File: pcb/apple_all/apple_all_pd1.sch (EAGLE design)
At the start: 47 parts, among them IC1 STM32F072C8T6, SW1 324_SW, SW2 324_SW, SW3 324_SW

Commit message: updated PCB
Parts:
- added TP1, TP2, TP3: PTR1TP14R, testpad:PTR1TP14R
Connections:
- new net N$10: IC1PORTB_L.PB5, JP2.2
- new net N$20: IC1PORTC.PC15, TP1.TP
- new net N$41: IC1PORTF/OSC.PF0/OSC<=, TP2.TP
- new net N$42: IC1PORTF/OSC.PF1/OSC=>, TP3.TP
- net N$24: no longer JP6.EARTH-NORM
- net N$46: no longer IC1PORTB_L.PB5, JP2.2
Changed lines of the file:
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@@
 <part name="R6" library="SparkFun-Passives" deviceset="RESISTOR" device="0805-RES" value="2K"/>
 <part name="R17" library="SparkFun-Passives" deviceset="RESISTOR" device="0805-RES" value="100"/>
+<part name="TP2" library="testpad" library_urn="urn:adsk.eagle:library:385" deviceset="PTR1" device="TP14R" package3d_urn="urn:adsk.eagle:package:27966/1"/>
+<part name="TP1" library="testpad" library_urn="urn:adsk.eagle:library:385" deviceset="PTR1" device="TP14R" package3d_urn="urn:adsk.eagle:package:27966/1"/>
+<part name="TP3" library="testpad" library_urn="urn:adsk.eagle:library:385" deviceset="PTR1" device="TP14R" package3d_urn="urn:adsk.eagle:package:27966/1"/>
 </parts>
 <sheets>
@@
 <attribute name="VALUE" x="339.09" y="9.398" size="1.778" layer="96"/>
 </instance>
+<instance part="TP2" gate="G$1" x="213.36" y="-2.54" smashed="yes" rot="R90">
+<attribute name="NAME" x="219.71" y="-3.556" size="1.778" layer="95" rot="R180"/>
+<attribute name="TP_SIGNAL_NAME" x="215.9" y="-1.27" size="1.778" layer="97" rot="R90"/>
+</instance>
+<instance part="TP1" gate="G$1" x="210.82" y="10.16" smashed="yes" rot="R90">
+<attribute name="NAME" x="217.17" y="9.144" size="1.778" layer="95" rot="R180"/>
+<attribute name="TP_SIGNAL_NAME" x="213.36" y="11.43" size="1.778" layer="97" rot="R90"/>
+</instance>
+<instance part="TP3" gate="G$1" x="228.6" y="-5.08" smashed="yes" rot="R90">
+<attribute name="NAME" x="234.95" y="-6.096" size="1.778" layer="95" rot="R180"/>
+<attribute name="TP_SIGNAL_NAME" x="231.14" y="-3.81" size="1.778" layer="97" rot="R90"/>
+</instance>
 </instances>
 <busses>
@@
 <wire x1="66.04" y1="93.98" x2="66.04" y2="111.76" width="0.1524" layer="91"/>
 <pinref part="JP2" gate="G$1" pin="1"/>
-<wire x1="66.04" y1="45.72" x2="66.04" y2="91.44" width="0.1524" layer="91"/>
-<pinref part="IC1" gate="PORTB_L" pin="PB5"/>
-<wire x1="43.18" y1="45.72" x2="66.04" y2="45.72" width="0.1524" layer="91"/>
-<pinref part="JP2" gate="G$1" pin="2"/>
-<wire x1="66.04" y1="93.98" x2="66.04" y2="91.44" width="0.1524" layer="91"/>
-<junction x="66.04" y="93.98"/>
-<junction x="66.04" y="91.44"/>
 <pinref part="R6" gate="G$1" pin="1"/>
 <wire x1="-7.62" y1="127" x2="-27.94" y2="127" width="0.1524" layer="91"/>
@@
 <pinref part="R13" gate="G$1" pin="1"/>
 <wire x1="294.64" y1="20.32" x2="297.18" y2="20.32" width="0.1524" layer="91"/>
-<pinref part="JP6" gate="G$1" pin="EARTH-NORM"/>
-<wire x1="294.64" y1="17.78" x2="294.64" y2="20.32" width="0.1524" layer="91"/>
-<junction x="294.64" y="20.32"/>
 </segment>
 </net>
@@
 </segment>
 </net>
+<net name="N$10" class="0">
+<segment>
+<pinref part="JP2" gate="G$1" pin="2"/>
+<wire x1="66.04" y1="45.72" x2="66.04" y2="91.44" width="0.1524" layer="91"/>
+<pinref part="IC1" gate="PORTB_L" pin="PB5"/>
+<wire x1="43.18" y1="45.72" x2="66.04" y2="45.72" width="0.1524" layer="91"/>
+</segment>
+</net>
+<net name="N$20" class="0">
+<segment>
+<pinref part="IC1" gate="PORTC" pin="PC15"/>
+<pinref part="TP1" gate="G$1" pin="TP"/>
+<wire x1="185.42" y1="10.16" x2="208.28" y2="10.16" width="0.1524" layer="91"/>
+</segment>
+</net>
+<net name="N$41" class="0">
+<segment>
+<pinref part="IC1" gate="PORTF/OSC" pin="PF0/OSC&lt;="/>
+<pinref part="TP2" gate="G$1" pin="TP"/>
+<wire x1="185.42" y1="-2.54" x2="210.82" y2="-2.54" width="0.1524" layer="91"/>
+</segment>
+</net>
+<net name="N$42" class="0">
+<segment>
+<pinref part="IC1" gate="PORTF/OSC" pin="PF1/OSC=&gt;"/>
+<pinref part="TP3" gate="G$1" pin="TP"/>
+<wire x1="185.42" y1="-5.08" x2="226.06" y2="-5.08" width="0.1524" layer="91"/>
+</segment>
+</net>

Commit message: updated values
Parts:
- R11, R7: value 200 -> 100
- R18, R21, R6, R9: value 2K -> 5.1K
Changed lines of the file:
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@@
 <part name="+3V16" library="backplane" deviceset="+3V3" device=""/>
 <part name="LED1" library="adafruit" deviceset="LED" device="CHIP-LED0805"/>
-<part name="R9" library="SparkFun-Passives" deviceset="RESISTOR" device="0805-RES" value="2K"/>
+<part name="R9" library="SparkFun-Passives" deviceset="RESISTOR" device="0805-RES" value="5.1K"/>
 <part name="GND9" library="backplane" deviceset="GND" device=""/>
 <part name="C1" library="clock" deviceset="CAP" device="0805" value="100nF"/>
@@
 <part name="C3" library="clock" deviceset="CAP" device="0805" value="100nF"/>
 <part name="LED2" library="adafruit" deviceset="LED" device="CHIP-LED0805"/>
-<part name="R18" library="SparkFun-Passives" deviceset="RESISTOR" device="0805-RES" value="2K"/>
+<part name="R18" library="SparkFun-Passives" deviceset="RESISTOR" device="0805-RES" value="5.1K"/>
 <part name="GND16" library="SparkFun-Aesthetics" deviceset="GND" device=""/>
 <part name="+3V10" library="backplane" deviceset="+3V3" device=""/>
@@
 <part name="U$3" library="adafruit_changed" deviceset="PINHD1X4" device=""/>
 <part name="LED3" library="adafruit" deviceset="LED" device="CHIP-LED0805"/>
-<part name="R21" library="SparkFun-Passives" deviceset="RESISTOR" device="0805-RES" value="2K"/>
+<part name="R21" library="SparkFun-Passives" deviceset="RESISTOR" device="0805-RES" value="5.1K"/>
 <part name="GND21" library="supply1" library_urn="urn:adsk.eagle:library:371" deviceset="GND" device=""/>
 <part name="GND22" library="supply1" library_urn="urn:adsk.eagle:library:371" deviceset="GND" device=""/>
@@
 <part name="SUPPLY7" library="supply2" library_urn="urn:adsk.eagle:library:372" deviceset="+7V" device=""/>
 <part name="JP1" library="pinhead" library_urn="urn:adsk.eagle:library:325" deviceset="PINHD-1X5" device="" package3d_urn="urn:adsk.eagle:package:22469/2"/>
-<part name="R7" library="SparkFun-Passives" deviceset="RESISTOR" device="0805-RES" value="200"/>
-<part name="R11" library="SparkFun-Passives" deviceset="RESISTOR" device="0805-RES" value="200"/>
+<part name="R7" library="SparkFun-Passives" deviceset="RESISTOR" device="0805-RES" value="100"/>
+<part name="R11" library="SparkFun-Passives" deviceset="RESISTOR" device="0805-RES" value="100"/>
 <part name="JP3" library="pinhead" library_urn="urn:adsk.eagle:library:325" deviceset="PINHD-2X2" device="" package3d_urn="urn:adsk.eagle:package:22455/2"/>
 <part name="JP7" library="adafruit" deviceset="PINHD-1X6" device="CB"/>
@@
 <part name="GND19" library="supply1" library_urn="urn:adsk.eagle:library:371" deviceset="GND" device=""/>
 <part name="JP2" library="pinhead" library_urn="urn:adsk.eagle:library:325" deviceset="PINHD-1X2" device="" package3d_urn="urn:adsk.eagle:package:22435/2"/>
-<part name="R6" library="SparkFun-Passives" deviceset="RESISTOR" device="0805-RES" value="2K"/>
+<part name="R6" library="SparkFun-Passives" deviceset="RESISTOR" device="0805-RES" value="5.1K"/>
 <part name="R17" library="SparkFun-Passives" deviceset="RESISTOR" device="0805-RES" value="100"/>
 <part name="TP2" library="testpad" library_urn="urn:adsk.eagle:library:385" deviceset="PTR1" device="TP14R" package3d_urn="urn:adsk.eagle:package:27966/1"/>

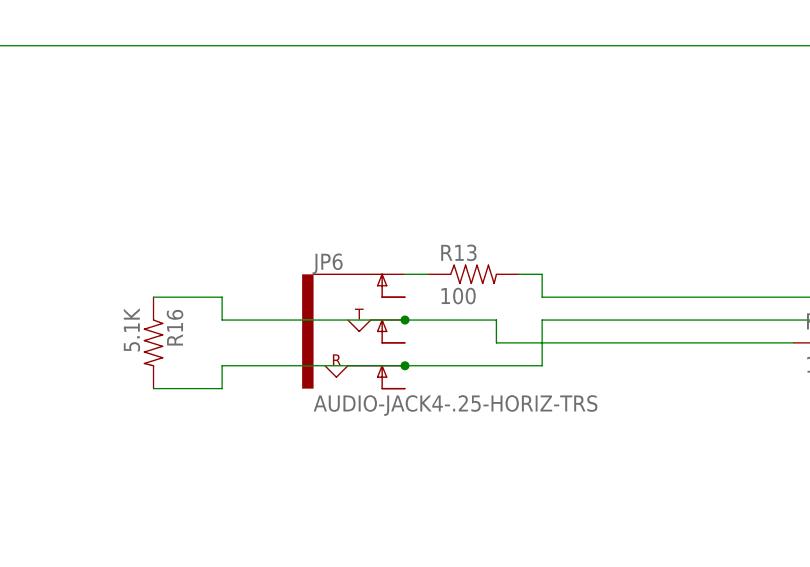
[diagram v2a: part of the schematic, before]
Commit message: moved resistors
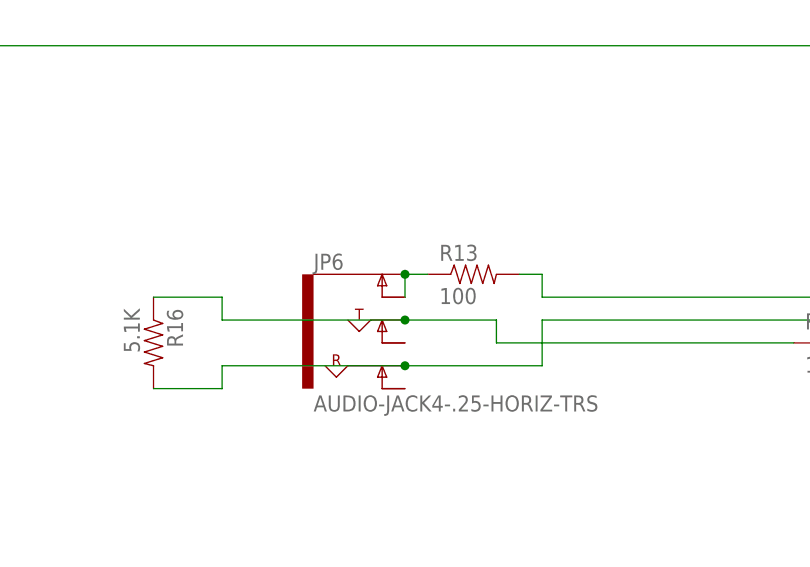
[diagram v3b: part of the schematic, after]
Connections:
- net N$24: now also JP6.EARTH-NORM
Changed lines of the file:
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@@
 <pinref part="R13" gate="G$1" pin="1"/>
 <wire x1="294.64" y1="20.32" x2="297.18" y2="20.32" width="0.1524" layer="91"/>
+<pinref part="JP6" gate="G$1" pin="EARTH-NORM"/>
+<wire x1="294.64" y1="17.78" x2="294.64" y2="20.32" width="0.1524" layer="91"/>
+<junction x="294.64" y="20.32"/>
 </segment>
 </net>

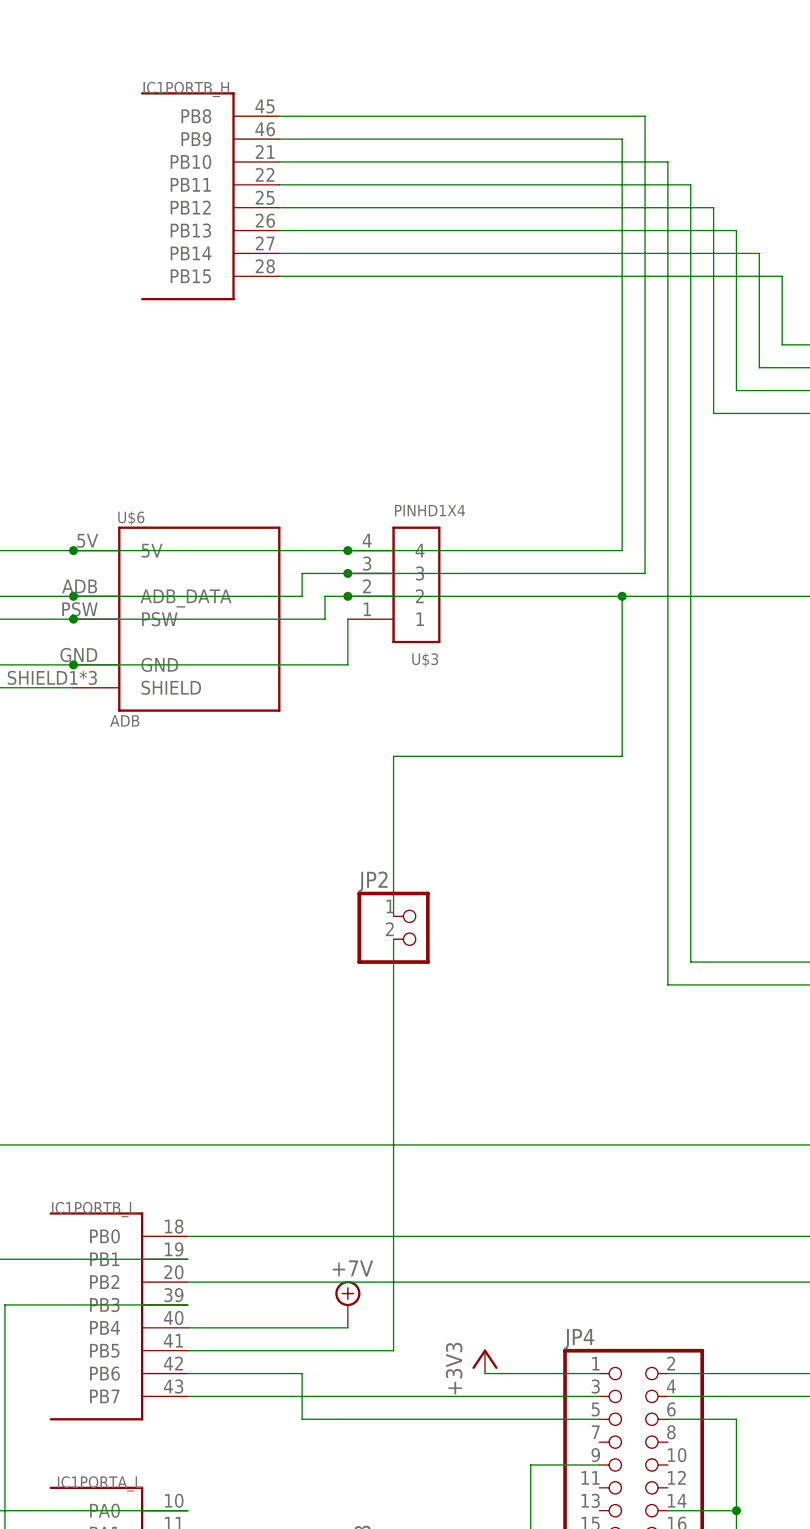
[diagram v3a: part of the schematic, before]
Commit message: added resistors on DET pins, cleaned up silkscreen
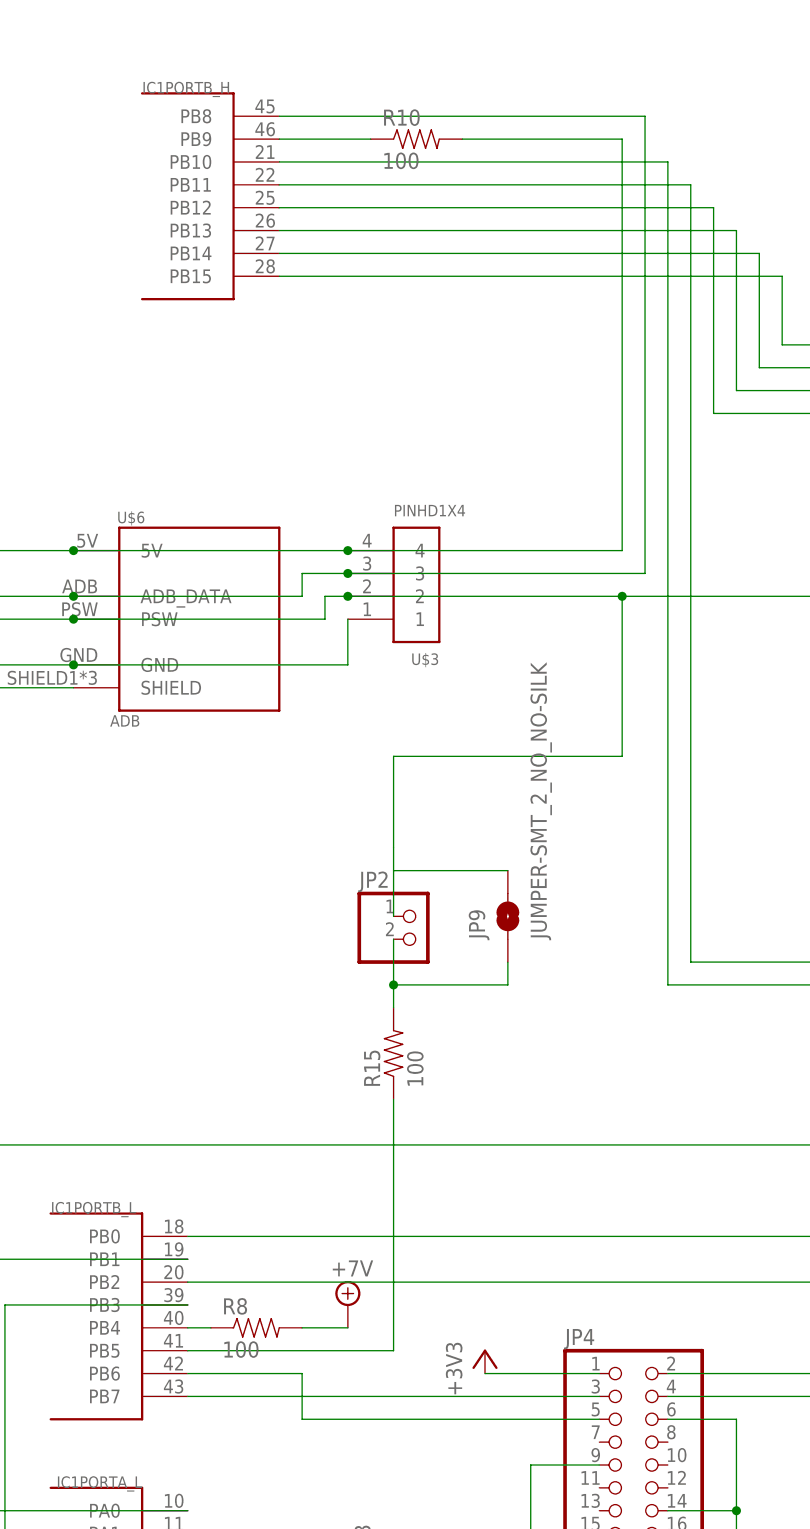
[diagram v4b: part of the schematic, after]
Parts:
- added JP9: JUMPER-SMT_2_NO_NO-SILK, SparkFun-Jumpers:JUMPER-SMT_2_NO_NO-SILK
- added R10, R15, R8: 100, SparkFun-Passives:RESISTOR0805-RES
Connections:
- new net N$44: IC1PORTB_L.PB4, R8.1
- new net N$45: IC1PORTB_H.PB9, R10.1
- new net N$47: JP2.2, JP9.1, R15.2
- net +7V: now also R8.2; no longer IC1PORTB_L.PB4
- net N$10: now also R15.1; no longer JP2.2
- net N$3: now also R10.2; no longer IC1PORTB_H.PB9
- net N$46: now also JP9.2
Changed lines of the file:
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@@
 <part name="TP1" library="testpad" library_urn="urn:adsk.eagle:library:385" deviceset="PTR1" device="TP14R" package3d_urn="urn:adsk.eagle:package:27966/1"/>
 <part name="TP3" library="testpad" library_urn="urn:adsk.eagle:library:385" deviceset="PTR1" device="TP14R" package3d_urn="urn:adsk.eagle:package:27966/1"/>
+<part name="R8" library="SparkFun-Passives" deviceset="RESISTOR" device="0805-RES" value="100"/>
+<part name="R10" library="SparkFun-Passives" deviceset="RESISTOR" device="0805-RES" value="100"/>
+<part name="R15" library="SparkFun-Passives" deviceset="RESISTOR" device="0805-RES" value="100"/>
+<part name="JP9" library="SparkFun-Jumpers" deviceset="JUMPER-SMT_2_NO" device="_NO-SILK"/>
 </parts>
 <sheets>
@@
 <attribute name="TP_SIGNAL_NAME" x="231.14" y="-3.81" size="1.778" layer="97" rot="R90"/>
 </instance>
+<instance part="R8" gate="G$1" x="50.8" y="48.26" smashed="yes">
+<attribute name="NAME" x="46.99" y="49.7586" size="1.778" layer="95"/>
+<attribute name="VALUE" x="46.99" y="44.958" size="1.778" layer="96"/>
+</instance>
+<instance part="R10" gate="G$1" x="68.58" y="180.34" smashed="yes">
+<attribute name="NAME" x="64.77" y="181.8386" size="1.778" layer="95"/>
+<attribute name="VALUE" x="64.77" y="177.038" size="1.778" layer="96"/>
+</instance>
+<instance part="R15" gate="G$1" x="66.04" y="78.74" smashed="yes" rot="R90">
+<attribute name="NAME" x="64.5414" y="74.93" size="1.778" layer="95" rot="R90"/>
+<attribute name="VALUE" x="69.342" y="74.93" size="1.778" layer="96" rot="R90"/>
+</instance>
+<instance part="JP9" gate="G$1" x="78.74" y="93.98" smashed="yes" rot="R90">
+<attribute name="NAME" x="76.2" y="91.44" size="1.778" layer="95" font="vector" rot="R90"/>
+<attribute name="VALUE" x="81.28" y="91.44" size="1.778" layer="96" font="vector" rot="R90" align="top-left"/>
+</instance>
 </instances>
 <busses>
@@
 <junction x="60.96" y="134.62"/>
 <wire x1="91.44" y1="134.62" x2="91.44" y2="180.34" width="0.1524" layer="91"/>
-<pinref part="IC1" gate="PORTB_H" pin="PB9"/>
-<wire x1="91.44" y1="180.34" x2="53.34" y2="180.34" width="0.1524" layer="91"/>
 <pinref part="R6" gate="G$1" pin="2"/>
 <wire x1="-7.62" y1="134.62" x2="-7.62" y2="137.16" width="0.1524" layer="91"/>
 <wire x1="-7.62" y1="137.16" x2="-27.94" y2="137.16" width="0.1524" layer="91"/>
 <junction x="-7.62" y="134.62"/>
+<wire x1="91.44" y1="180.34" x2="73.66" y2="180.34" width="0.1524" layer="91"/>
+<pinref part="R10" gate="G$1" pin="2"/>
 </segment>
 </net>
@@
 <junction x="91.44" y="129.54"/>
 <junction x="152.4" y="129.54"/>
-<wire x1="66.04" y1="93.98" x2="66.04" y2="111.76" width="0.1524" layer="91"/>
+<wire x1="66.04" y1="93.98" x2="66.04" y2="99.06" width="0.1524" layer="91"/>
 <pinref part="JP2" gate="G$1" pin="1"/>
 <pinref part="R6" gate="G$1" pin="1"/>
+<wire x1="66.04" y1="101.6" x2="66.04" y2="111.76" width="0.1524" layer="91"/>
 <wire x1="-7.62" y1="127" x2="-27.94" y2="127" width="0.1524" layer="91"/>
 <junction x="-7.62" y="127"/>
+<pinref part="JP9" gate="G$1" pin="2"/>
+<wire x1="78.74" y1="99.06" x2="66.04" y2="99.06" width="0.1524" layer="91"/>
+<wire x1="66.04" y1="99.06" x2="66.04" y2="101.6" width="0.1524" layer="91"/>
 </segment>
 </net>
@@
 </segment>
 <segment>
-<pinref part="IC1" gate="PORTB_L" pin="PB4"/>
-<wire x1="43.18" y1="48.26" x2="60.96" y2="48.26" width="0.1524" layer="91"/>
 <pinref part="SUPPLY1" gate="G$1" pin="+7V"/>
+<wire x1="55.88" y1="48.26" x2="60.96" y2="48.26" width="0.1524" layer="91"/>
+<pinref part="R8" gate="G$1" pin="2"/>
 </segment>
 </net>
@@
 <net name="N$10" class="0">
 <segment>
-<pinref part="JP2" gate="G$1" pin="2"/>
-<wire x1="66.04" y1="45.72" x2="66.04" y2="91.44" width="0.1524" layer="91"/>
 <pinref part="IC1" gate="PORTB_L" pin="PB5"/>
 <wire x1="43.18" y1="45.72" x2="66.04" y2="45.72" width="0.1524" layer="91"/>
+<wire x1="66.04" y1="45.72" x2="66.04" y2="73.66" width="0.1524" layer="91"/>
+<pinref part="R15" gate="G$1" pin="1"/>
 </segment>
 </net>
@@
 </segment>
 </net>
+<net name="N$44" class="0">
+<segment>
+<pinref part="IC1" gate="PORTB_L" pin="PB4"/>
+<wire x1="43.18" y1="48.26" x2="45.72" y2="48.26" width="0.1524" layer="91"/>
+<pinref part="R8" gate="G$1" pin="1"/>
+</segment>
+</net>
+<net name="N$45" class="0">
+<segment>
+<pinref part="IC1" gate="PORTB_H" pin="PB9"/>
+<wire x1="63.5" y1="180.34" x2="53.34" y2="180.34" width="0.1524" layer="91"/>
+<pinref part="R10" gate="G$1" pin="1"/>
+</segment>
+</net>
+<net name="N$47" class="0">
+<segment>
+<pinref part="JP2" gate="G$1" pin="2"/>
+<wire x1="66.04" y1="83.82" x2="66.04" y2="86.36" width="0.1524" layer="91"/>
+<pinref part="R15" gate="G$1" pin="2"/>
+<pinref part="JP9" gate="G$1" pin="1"/>
+<wire x1="66.04" y1="86.36" x2="66.04" y2="91.44" width="0.1524" layer="91"/>
+<wire x1="78.74" y1="88.9" x2="78.74" y2="86.36" width="0.1524" layer="91"/>
+<wire x1="78.74" y1="86.36" x2="66.04" y2="86.36" width="0.1524" layer="91"/>
+<junction x="66.04" y="86.36"/>
+</segment>
+</net>
